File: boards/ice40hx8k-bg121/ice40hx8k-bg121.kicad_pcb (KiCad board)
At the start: 4 copper layers, 22.9 x 48.3 mm, 60 parts, among them J1 Conn_01x16, J2 Conn_01x16, J3 Conn_02x06_Odd_Even, J4 Conn_02x06_Odd_Even, SW1 B3U-1000P, U1 AP7361C-33Y5-13, U2 AP7361C-12Y5-13, U3 iCE40HX8K-BG121(121-Ball_caBG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, U4 LE25U20AMB, U5 ASDMB-xxxMHz

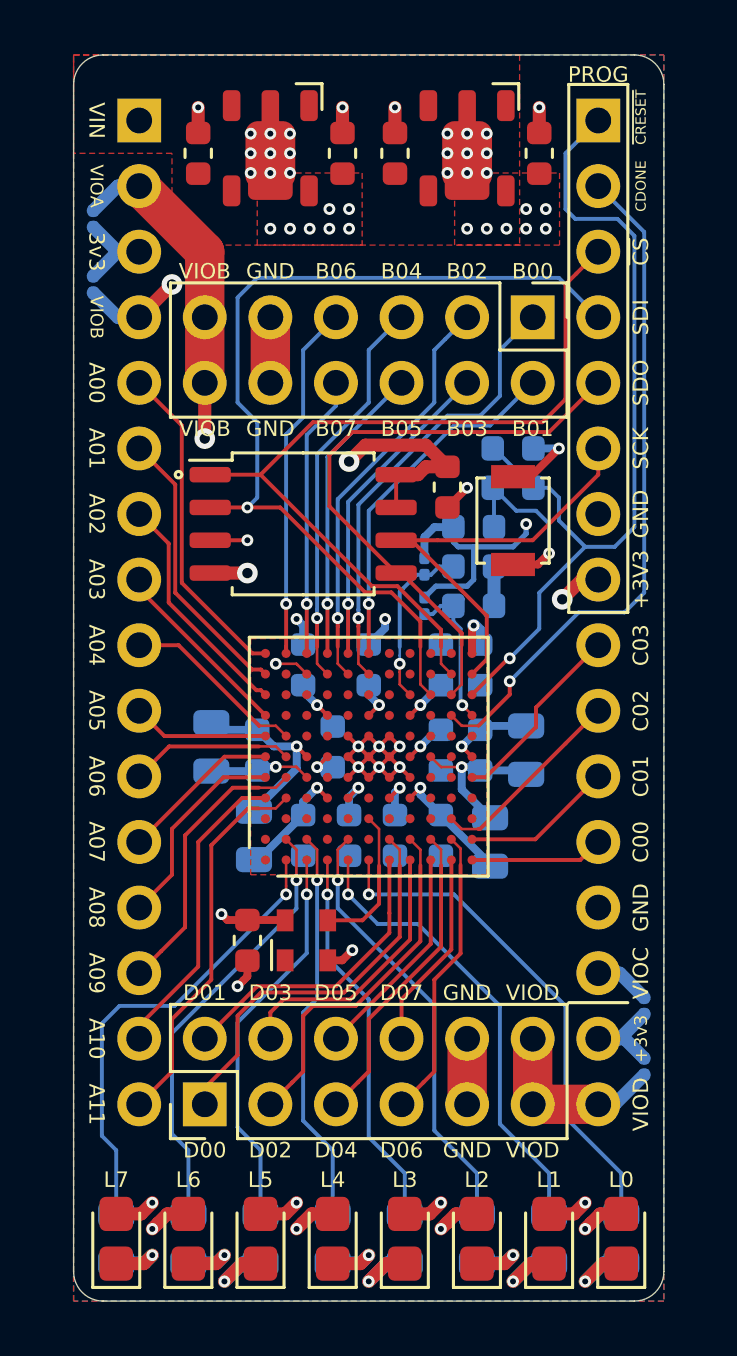
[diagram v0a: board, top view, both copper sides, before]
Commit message: Updated pinout to add PMOD and VCCIOA/B options.
* Added castillated pads.
* Length matched IOs (20mm)
* ... and more!
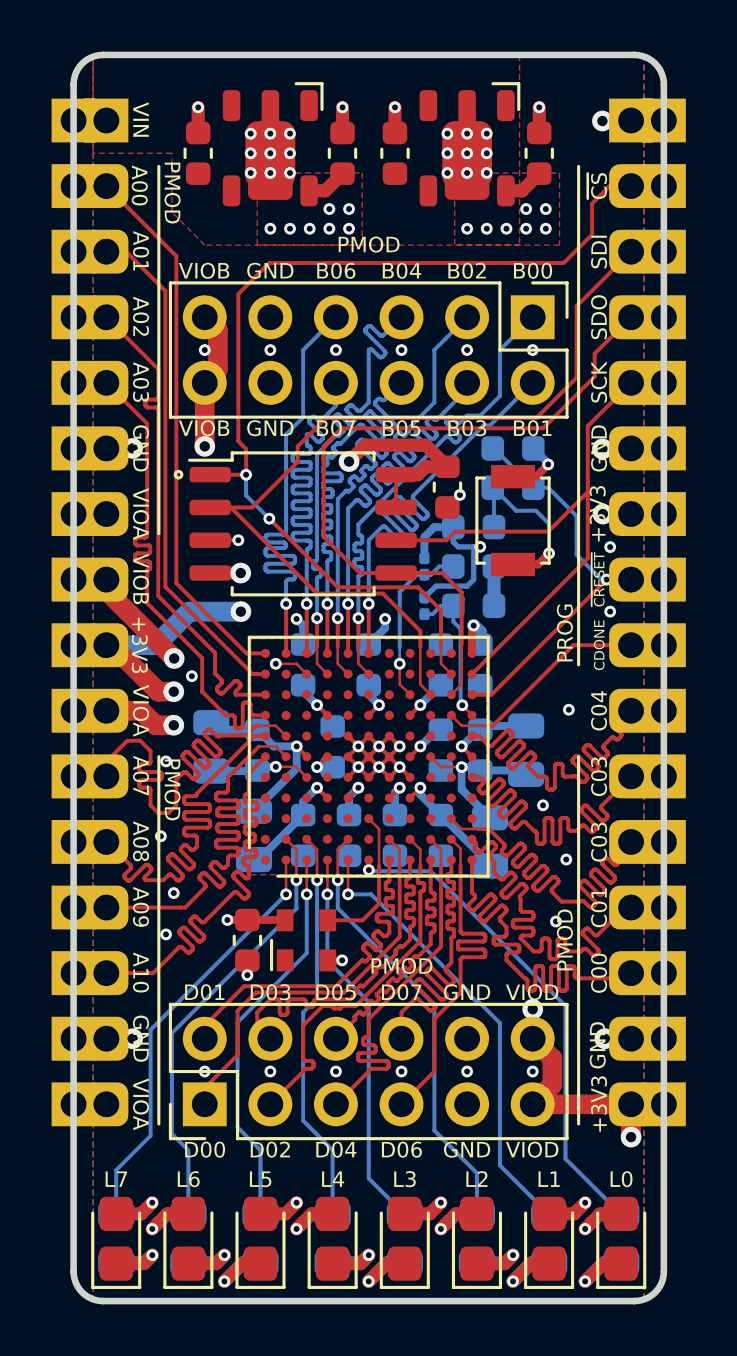
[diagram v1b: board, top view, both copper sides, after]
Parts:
- removed JP3: VCCIO_A, jkiv-library:J_NO_0201_0603Metric
- removed JP4: VCCIO_B, jkiv-library:J_NO_0201_0603Metric
- removed JP5: VCCIO_C, jkiv-library:J_NO_0201_0603Metric
- removed JP6: VCCIO_D, jkiv-library:J_NO_0201_0603Metric
- removed REF**: OSHW-Symbol_6.7x6mm_SilkScreen, Symbol:OSHW-Symbol_6.7x6mm_SilkScreen
- R12, R14: value 10k -> 1k
- moved J1 1.27 mm to (21.6, 17.8)
- moved J2 1.27 mm to (41.9, 17.8)
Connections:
- C16 pad 2: VCCIO_D -> VCCIO_C
- C17 pad 2: VCCIO_D -> VCCIO_C
- C18 pad 2: +3V3 -> VCCIO_C
- C19 pad 2: +3V3 -> VCCIO_C
- C2 pad 1: +3V3 -> VCCIO_C
- C21 pad 2: +3V3 -> VCCIO_C
- D10 pad 2: +3V3 -> VCCIO_C
- D3 pad 2: +3V3 -> VCCIO_C
- D4 pad 2: +3V3 -> VCCIO_C
- D5 pad 2: +3V3 -> VCCIO_C
- D6 pad 2: +3V3 -> VCCIO_C
- D7 pad 2: +3V3 -> VCCIO_C
- D8 pad 2: +3V3 -> VCCIO_C
- D9 pad 2: +3V3 -> VCCIO_C
- J1 pad 10: IO_A05 -> VCCIO_A
- J1 pad 11: IO_A06 -> IO_A04
- J1 pad 12: IO_A07 -> IO_A05
- J1 pad 13: IO_A08 -> IO_A06
- J1 pad 14: IO_A09 -> IO_A07
- J1 pad 15: IO_A10 -> GND
- J1 pad 16: IO_A11 -> VCCIO_A
- J1 pad 2: VCCIO_B -> IO_A00
- J1 pad 3: +3V3 -> IO_A01
- J1 pad 4: VCCIO_A -> IO_A02
- J1 pad 5: IO_A00 -> IO_A03
- J1 pad 6: IO_A01 -> GND
- J1 pad 7: IO_A02 -> VCCIO_A
- J1 pad 8: IO_A03 -> VCCIO_B
- J1 pad 9: IO_A04 -> VCCIO_C
- J2 pad 1: PROG_CRESET_B -> VCCIO_C
- J2 pad 10: IO_C02 -> IO_C04
- J2 pad 11: IO_C01 -> IO_C03
- J2 pad 12: IO_C00 -> IO_C02
- J2 pad 13: GND -> IO_C01
- J2 pad 14: VCCIO_C -> IO_C00
- J2 pad 15: +3V3 -> GND
- J2 pad 16: VCCIO_D -> VCCIO_C
- J2 pad 2: CDONE -> PROG_SS_B
- J2 pad 3: PROG_SS_B -> PROG_SDI
- J2 pad 4: PROG_SDI -> PROG_SDO
- J2 pad 5: PROG_SDO -> PROG_SCK
- J2 pad 6: PROG_SCK -> GND
- J2 pad 7: GND -> VCCIO_C
- J2 pad 8: +3V3 -> PROG_CRESET_B
- J2 pad 9: IO_C03 -> CDONE
- J3 pad 11: VCCIO_D -> VCCIO_C
- J3 pad 12: VCCIO_D -> VCCIO_C
- JP1 pad 2: +3V3 -> VCCIO_C
- JP2 pad 1: +3V3 -> VCCIO_C
- R14 pad 1: +3V3 -> VCCIO_C
- U1 pad 5: +3V3 -> VCCIO_C
- U3 pad C10: +3V3 -> VCCIO_C
- U3 pad E4: VCCIO_D -> VCCIO_C
- U3 pad G4: VCCIO_D -> VCCIO_C
- U3 pad L11: +3V3 -> VCCIO_C
- U3 pad L7: Net-(U3-PadL7) -> IO_C04
- U4 pad 3: +3V3 -> VCCIO_C
- U4 pad 7: +3V3 -> VCCIO_C
- U4 pad 8: +3V3 -> VCCIO_C
- U5 pad 4: +3V3 -> VCCIO_C
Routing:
- net VCCIO_C: track 18.1 -> 84.9 mm, vias 1 -> 30
- net +3V3: track 47.1 -> 0.00 mm, vias 22 -> 0
- net VCCIO_D: track 25.5 -> 0.00 mm, vias 2 -> 0
- net IO_C04: track 0.00 -> 19.8 mm
- net CDONE: track 26.6 -> 9.22 mm, vias 1 -> 0
- net PROG_CRESET_B: track 33.8 -> 17.2 mm
- net IO_A05: track 5.30 -> 21.4 mm
- net IO_C00: track 5.18 -> 20.8 mm
- net IO_A11: track 14.8 -> 0.00 mm
- net IO_A07: track 6.26 -> 20.8 mm
- net IO_A06: track 6.34 -> 20.8 mm
- net IO_C01: track 5.90 -> 20.4 mm
- net IO_A04: track 7.15 -> 20.8 mm
- net IO_A03: track 7.28 -> 20.8 mm
- net IO_C03: track 7.46 -> 20.8 mm
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- added copper zone on F.Cu, net VCCIO_C
- added copper zone on In1.Cu, net VCCIO_C
- removed copper zone on F.Cu, net +3V3
- removed copper zone on In1.Cu, net +3V3
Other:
- board text added: "C04"
- board text added: "PMOD"
- board text removed: "+3v3"
- board text removed: "3v3"
- board text removed: "A04"
- board text removed: "A05"
- board text removed: "A06"
- board text removed: "A11"
- board text removed: "C02"
- board text removed: "VIOC"
